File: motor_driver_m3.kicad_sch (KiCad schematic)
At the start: 31 parts, among them J10 Conn_01x01_Pin, J11 Conn_01x01_Pin, J12 Conn_01x01_Pin, M3 DRV8320SRTVR, Q13 NP80N06D6, Q14 NP80N06D6, Q15 NP80N06D6, Q16 NP80N06D6, Q17 NP80N06D6, Q18 NP80N06D6

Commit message: ...
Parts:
- C36: renamed from C33; footprint easyeda2kicad:C0603 -> easyeda2kicad:C0402
- renumbered C32 to C35, C34 to C37, C35 to C38, C36 to C39, C37 to C40, C38 to C41, C39 to C42, J11 to J10, J12 to J11, J10 to J12, R44 to R36, R45 to R37, R46 to R38, R47 to R39, R48 to R40, R49 to R41, R50 to R42, R51 to R43, R52 to R44, R53 to R45, R54 to R46, R55 to R47, R56 to R48
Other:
- moved on the sheet: J11, J12

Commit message: ...
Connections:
- net SCLK: no longer names the net of M3.20 (SCLK)
- net SDI: no longer names the net of M3.19 (SDI)
- net SDO: no longer names the net of M3.18 (SDO)
- no-connect marks 0 -> 3
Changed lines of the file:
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@@
 		(color 0 0 0 0)
 	)
+	(no_connect
+		(at 92.71 80.01)
+	)
+	(no_connect
+		(at 92.71 74.93)
+	)
+	(no_connect
+		(at 92.71 77.47)
+	)
 	(wire
 		(pts
@@
 	(wire
 		(pts
-			(xy 105.41 74.93) (xy 92.71 74.93)
-		)
-		(stroke
-			(width 0)
-			(type default)
-		)
-	)
-	(wire
-		(pts
 			(xy 252.73 153.67) (xy 250.19 153.67)
 		)
@@
 	(wire
 		(pts
-			(xy 105.41 77.47) (xy 92.71 77.47)
-		)
-		(stroke
-			(width 0)
-			(type default)
-		)
-	)
-	(wire
-		(pts
 			(xy 252.73 52.07) (xy 250.19 52.07)
 		)
@@
 	(wire
 		(pts
-			(xy 92.71 80.01) (xy 105.41 80.01)
-		)
-		(stroke
-			(width 0)
-			(type default)
-		)
-	)
-	(wire
-		(pts
 			(xy 21.59 50.8) (xy 21.59 49.53)
 		)
@@
 		)
 	)
-	(global_label "SCLK"
-		(shape input)
-		(at 105.41 74.93 0)
-		(fields_autoplaced yes)
-		(effects
-			(font
-				(size 1.27 1.27)
-			)
-			(justify left)
-		)
-		(property "Intersheetrefs" "${INTERSHEET_REFS}"
-			(at 113.1728 74.93 0)
-			(effects
-				(font
-					(size 1.27 1.27)
-				)
-				(justify left)
-				(hide yes)
-			)
-		)
-	)
 	(global_label "SHB3"
 		(shape input)
@@
 		)
 	)
-	(global_label "SDI"
-		(shape input)
-		(at 105.41 77.47 0)
-		(fields_autoplaced yes)
-		(effects
-			(font
-				(size 1.27 1.27)
-			)
-			(justify left)
-		)
-		(property "Intersheetrefs" "${INTERSHEET_REFS}"
-			(at 111.4795 77.47 0)
-			(effects
-				(font
-					(size 1.27 1.27)
-				)
-				(justify left)
-				(hide yes)
-			)
-		)
-	)
 	(global_label "B+"
 		(shape input)
@@
 			(effects
 				(font
-					(size 1.27 1.27)
-				)
-				(justify left)
-				(hide yes)
-			)
-		)
-	)
-	(global_label "SDO"
-		(shape input)
-		(at 105.41 80.01 0)
-		(fields_autoplaced yes)
-		(effects
-			(font
-				(size 1.27 1.27)
-			)
-			(justify left)
-		)
-		(property "Intersheetrefs" "${INTERSHEET_REFS}"
-			(at 112.2052 80.01 0)
-			(effects
-				(font

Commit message: ...
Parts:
- added C53: 100nF, easyeda2kicad:C0603, symbol Device:C
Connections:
- net B+: now also C53.1
- net GND: now also C53.2
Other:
- moved on the sheet: C40, C41, C42, J10, J11, J12, R43, R44, R45, R46, R47, R48

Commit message: complete change in architecture,work in progress
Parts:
- removed M3: DRV8320SRTVR, easyeda2kicad:WQFN-32_L5.0-W5.0-P0.50-TL-EP3.5, symbol easyeda2kicad:DRV8320SRTVR
- added C45: 4.7uF, easyeda2kicad:C0402, symbol Device:C
- added C46, C47, C57: 1uF, easyeda2kicad:C0402, symbol Device:C
- added C60, C61: 100nF, easyeda2kicad:C0603, symbol Device:C
- added J19: Conn_01x01_Pin, deshan:Conn_1x1_small, symbol Connector:Conn_01x01_Pin
- added R70: 39k, easyeda2kicad:R0402, symbol Device:R
- added R71, R72, R73: 10k, easyeda2kicad:R0402, symbol Device:R
- added R74: 50k, easyeda2kicad:R0402, symbol Device:R
- added U8: STDRIVE101, easyeda2kicad:QFN-24_L4.0-W4.0-P0.50-BL-EP2.7, symbol easyeda2kicad:STDRIVE101
- added U9: STM32C011F6U6TR, easyeda2kicad:UFQFPN-20_L3.0-W3.0-P0.50-TL, symbol easyeda2kicad:STM32C011F6U6TR
- C35: value >10uF -> 100nF
- C36: value 0.1uF -> 100nF
- C37, C39: value 1uF -> 100nF; footprint easyeda2kicad:C0603 -> easyeda2kicad:C0402
- C38: value 47nF -> 4.7uF
- R36: value 10k -> 18k
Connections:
- net 3V3: now also C37.1, R36.1, C45.1, R70.2, R71.2, U9.2 (VDD/VDDA); no longer R36.2
- net B+: now also C60.1, C61.1, U8.4 (VS); no longer C35.1, C37.1
- net GND: now also C37.2, C38.2, C45.2, C60.2, C61.2, R72.2, R73.1, R74.2, U8.25 (EP), U9.3 (VSS/VSSA); no longer R38.2, R40.2, R42.2
- net at C38.1: now also C35.1, U8.5 (REG12)
- net at C39.1: now also R71.1, U9.4 (PF2-NRST)
- net GHA3: no longer names the net of Q13.4 (G), R37.1
- net GHB3: no longer names the net of Q15.4 (G), R39.1
- net GHC3: no longer names the net of Q17.4 (G), R41.1
- net GLA3: no longer names the net of Q14.4 (G), R38.1
- net GLB3: no longer names the net of Q16.4 (G), R40.1
- net GLC3: no longer names the net of Q18.4 (G), R42.1
- net SHA3 renamed OUT1
- net OUT1: now also C46.1, U8.23 (OUT1); no longer R37.2
- net SHB3 renamed OUT2
- net OUT2: now also C47.1, U8.19 (OUT2); no longer R39.2
- net SHC3 renamed OUT3
- net OUT3: now also C57.1, U8.15 (OUT3); no longer R41.2
- new net: R73.2, U8.1 (CP)
- new net: C57.2, U8.13 (BOOT3)
- new net: C47.2, U8.17 (BOOT2)
- new net: R74.1, U8.2 (DT/MODE)
- new net: C46.2, U8.21 (BOOT1)
- new net: R36.2, R72.1, U8.3 (SCREF)
- new net: R70.1, U8.6 (nFAULT)
- new net DShot_M3: J19.1 (Pin_1)
- new net EN1_M3: U8.10 (INL1/EN1), U9.12 (PA7)
- new net EN2_M3: U8.11 (INL2/EN2), U9.11 (PA6)
- new net EN3_M3: U8.12 (INL3/EN3), U9.10 (PA5)
- new net GHS1: R37.2, U8.22 (GHS1)
- new net GHS2: R39.2, U8.18 (GHS2)
- new net GHS3: R41.2, U8.14 (GHS3)
- new net GLS1: R38.2, U8.24 (GLS1)
- new net GLS2: R40.2, U8.20 (GLS2)
- new net GLS3: R42.2, U8.16 (GLS3)
- new net INH1_M3: U8.7 (INH1/IN1), U9.15 (PA12[PA10])
- new net INH2_M3: U8.8 (INH2/IN2), U9.14 (PA11[PA9])
- new net INH3_M3: U8.9 (INH3/IN3), U9.13 (PA8)
- new net SWCLK: U9.17 (PA14-BOOT0)
- new net SWDIO_M3: U9.16 (PA13)
- no-connect marks 3 -> 2
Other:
- moved on the sheet: C40, C41, C42, C53, J10, J11, J12, R37, R38, R39, R40, R41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

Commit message: ...
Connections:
- net DShot_M3: now also U9.6 (PA1)
- net PHASE_A_M1: now also U9.8 (PA3)
- net PHASE_B_M1: now also U9.7 (PA2)
- net PHASE_C_M1: now also U9.9 (PA4)
- net SWCLK renamed SWCLK_H
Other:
- title: (none) -> MOTOR DRIVER M3
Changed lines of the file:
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@@
 	(generator_version "10.0")
 	(paper "A4")
+	(title_block
+		(title "MOTOR DRIVER M3")
+		(rev "1.0")
+	)
 	(text_box "DShot\n"
 		(exclude_from_sim no)
@@
 		)
 	)
+	(global_label "DShot_M3"
+		(shape input)
+		(at 68.58 57.15 180)
+		(fields_autoplaced yes)
+		(effects
+			(font
+				(size 1.27 1.27)
+			)
+			(justify right)
+		)
+		(property "Intersheetrefs" "${INTERSHEET_REFS}"
+			(at 56.4631 57.15 0)
+			(hide yes)
+			(show_name no)
+			(do_not_autoplace no)
+			(effects
+				(font
+					(size 1.27 1.27)
+				)
+				(justify right)
+			)
+		)
+	)
 	(global_label "OUT2"
 		(shape input)
@@
 	(global_label "PHASE_A_M1"
 		(shape input)
-		(at 144.78 31.75 180)
+		(at 68.58 62.23 180)
 		(fields_autoplaced yes)
 		(effects
@@
 		)
 		(property "Intersheetrefs" "${INTERSHEET_REFS}"
-			(at 130.0625 31.75 0)
+			(at 53.8625 62.23 0)
 			(hide yes)
 			(show_name no)
@@
 		)
 	)
-	(global_label "SWCLK"
+	(global_label "SWCLK_H"
 		(shape input)
 		(at 121.92 52.07 0)
@@
 		)
 		(property "Intersheetrefs" "${INTERSHEET_REFS}"
-			(at 131.1342 52.07 0)
+			(at 133.4323 52.07 0)
 			(hide yes)
 			(show_name no)
@@
 	(global_label "PHASE_B_M1"
 		(shape input)
-		(at 144.78 29.21 180)
+		(at 68.58 59.69 180)
 		(fields_autoplaced yes)
 		(effects
@@
 		)
 		(property "Intersheetrefs" "${INTERSHEET_REFS}"
-			(at 129.8811 29.21 0)
+			(at 53.6811 59.69 0)
 			(hide yes)
 			(show_name no)
@@
 	(global_label "PHASE_C_M1"
 		(shape input)
-		(at 144.78 34.29 180)
+		(at 68.58 64.77 180)
 		(fields_autoplaced yes)
 		(effects
@@
 		)
 		(property "Intersheetrefs" "${INTERSHEET_REFS}"
-			(at 129.8811 34.29 0)
-			(hide yes)
-			(show_name no)
+			(at 53.6811 64.77 0)
+			(hide yes)
+			(show_name no)

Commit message: ...
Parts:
- J10, J11, J12: footprint deshan:Conn_1x1 -> deshan:Conn_01x01_Power
- J19: footprint deshan:Conn_1x1_small -> deshan:Conn_01x01_Pin
- renumbered C39 to C31, C37 to C32, C45 to C33, C36 to C34, C38 to C36, C46 to C37, C47 to C38, C57 to C39, C53 to C40, C61 to C41, C60 to C42, C40 to C43, C41 to C44, C42 to C45, R71 to R37, R36 to R38, R72 to R39, R73 to R40, R74 to R41, R70 to R42, R37 to R43, R38 to R44, R39 to R45, R40 to R46, R41 to R47, R42 to R48, R43 to R49, R44 to R50, R45 to R51, R46 to R52, R47 to R53, R48 to R54
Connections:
- net PHASE_A_M1 is gone; now on net PHASE_B_M3: U9.8 (PA3)
- net PHASE_B_M1 is gone; now on net PHASE_C_M3: U9.7 (PA2)
- net PHASE_C_M1 is gone; now on net PHASE_A_M3: U9.9 (PA4)
- net SWCLK_H renamed SWCLK_M3

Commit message: ...
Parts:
- renumbered J19 to DShot_M3, U8 to GD3, J10 to J7, J11 to J8, J12 to J9, U9 to M3
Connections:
- no-connect marks 2 -> 5
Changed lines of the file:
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@@
 	)
 	(no_connect
+		(at 121.92 49.53)
+	)
+	(no_connect
+		(at 68.58 54.61)
+	)
+	(no_connect
 		(at 68.58 44.45)
 	)
 	(no_connect
+		(at 121.92 46.99)
+	)
+	(no_connect
 		(at 121.92 44.45)
 	)
@@
 		(dnp no)
 		(fields_autoplaced yes)
-		(property "Reference" "U8"
+		(property "Reference" "GD3"
 			(at 85.09 95.25 0)
 			(show_name no)
@@
 			(project "esc"
 				(path "/131092d7-5dad-4272-a758-a2445b6ec99c/01ceff22-9ba4-449c-a4ee-d6fe6e674f35"
-					(reference "U8")
+					(reference "GD3")
 					(unit 1)
 				)
@@
 		(dnp no)
 		(fields_autoplaced yes)
-		(property "Reference" "U9"
+		(property "Reference" "M3"
 			(at 95.25 36.83 0)
 			(show_name no)
@@
 			(project "esc"
 				(path "/131092d7-5dad-4272-a758-a2445b6ec99c/01ceff22-9ba4-449c-a4ee-d6fe6e674f35"
-					(reference "U9")
+					(reference "M3")
 					(unit 1)
 				)
@@
 		(dnp no)
 		(fields_autoplaced yes)
-		(property "Reference" "J10"
+		(property "Reference" "J7"
 			(at 154.305 163.83 0)
 			(show_name no)
@@
 			(project "esc"
 				(path "/131092d7-5dad-4272-a758-a2445b6ec99c/01ceff22-9ba4-449c-a4ee-d6fe6e674f35"
-					(reference "J10")
+					(reference "J7")
 					(unit 1)
 				)
@@
 		(dnp no)
 		(fields_autoplaced yes)
-		(property "Reference" "J12"
+		(property "Reference" "J9"
 			(at 154.305 181.61 0)
 			(show_name no)
@@
 			(project "esc"
 				(path "/131092d7-5dad-4272-a758-a2445b6ec99c/01ceff22-9ba4-449c-a4ee-d6fe6e674f35"
-					(reference "J12")
+					(reference "J9")
 					(unit 1)
 				)
@@
 		(dnp no)
 		(fields_autoplaced yes)
-		(property "Reference" "J19"
+		(property "Reference" "DShot_M3"
 			(at 168.91 130.1749 90)
 			(show_name no)
@@
 			(project "esc"
 				(path "/131092d7-5dad-4272-a758-a2445b6ec99c/01ceff22-9ba4-449c-a4ee-d6fe6e674f35"
-					(reference "J19")
+					(reference "DShot_M3")
 					(unit 1)
 				)
@@
 		(dnp no)
 		(fields_autoplaced yes)
-		(property "Reference" "J11"
+		(property "Reference" "J8"
 			(at 154.305 172.72 0)
 			(show_name no)
@@
 			(project "esc"
 				(path "/131092d7-5dad-4272-a758-a2445b6ec99c/01ceff22-9ba4-449c-a4ee-d6fe6e674f35"
-					(reference "J11")
+					(reference "J8")
 					(unit 1)
 				)

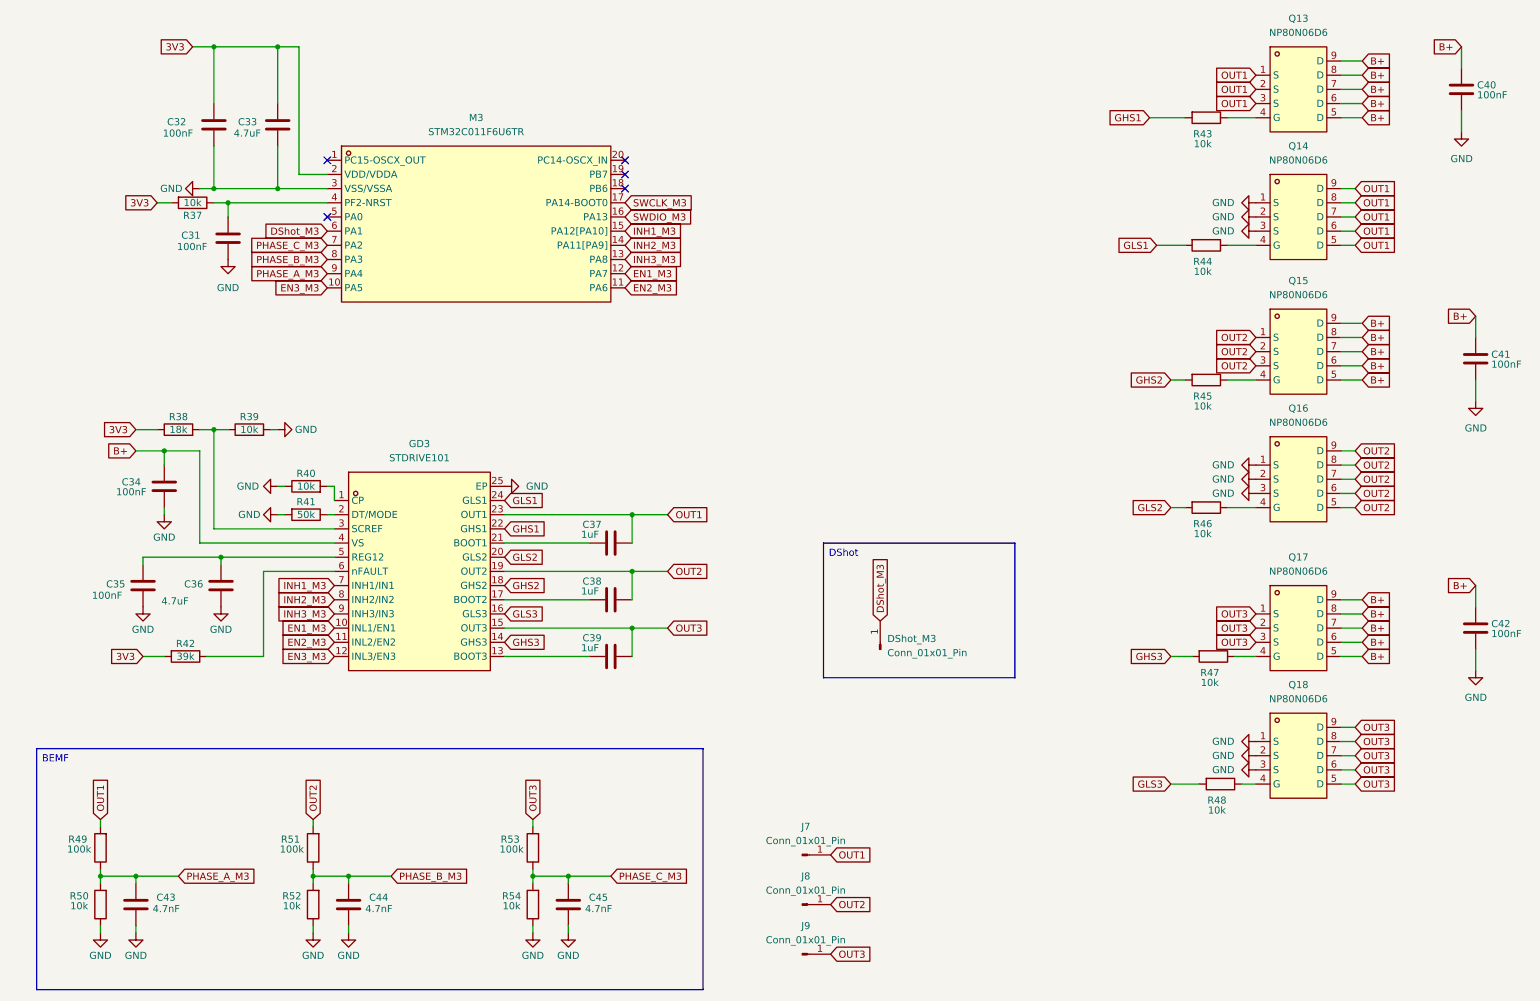
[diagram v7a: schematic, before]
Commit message: change in architecture with horizonatal half bridge
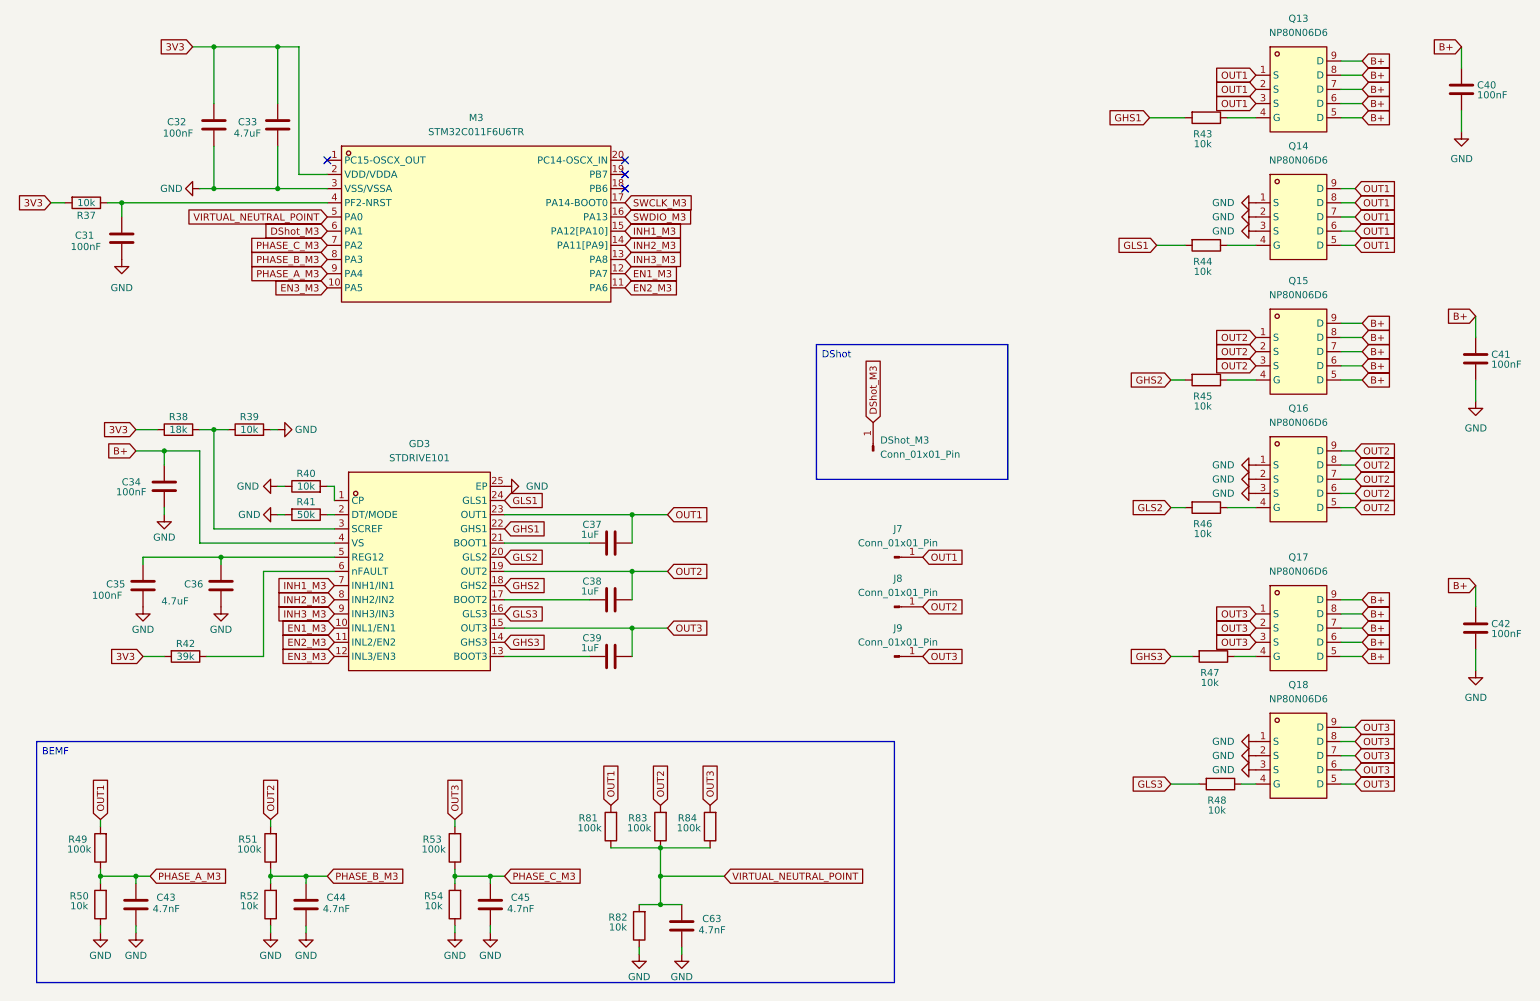
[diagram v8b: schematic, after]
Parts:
- added C63: 4.7nF, easyeda2kicad:C0402, symbol Device:C
- added R81, R83, R84: 100k, easyeda2kicad:R0402, symbol Device:R
- added R82: 10k, easyeda2kicad:R0402, symbol Device:R
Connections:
- net GND: now also C63.2, R82.1
- net OUT1: now also R81.2
- net OUT2: now also R83.2
- net OUT3: now also R84.2
- net VIRTUAL_NEUTRAL_POINT: now reaches M3.5 (PA0)
- net VIRTUAL_NEUTRAL_POINT: now also C63.1, R81.1, R82.2, R83.1, R84.1
- no-connect marks 5 -> 4
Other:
- moved on the sheet: C31, C44, C45, DShot_M3, J7, J8, J9, R37, R51, R52, R53, R54
